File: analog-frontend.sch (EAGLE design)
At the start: 3 parts, among them IC1 ADG731

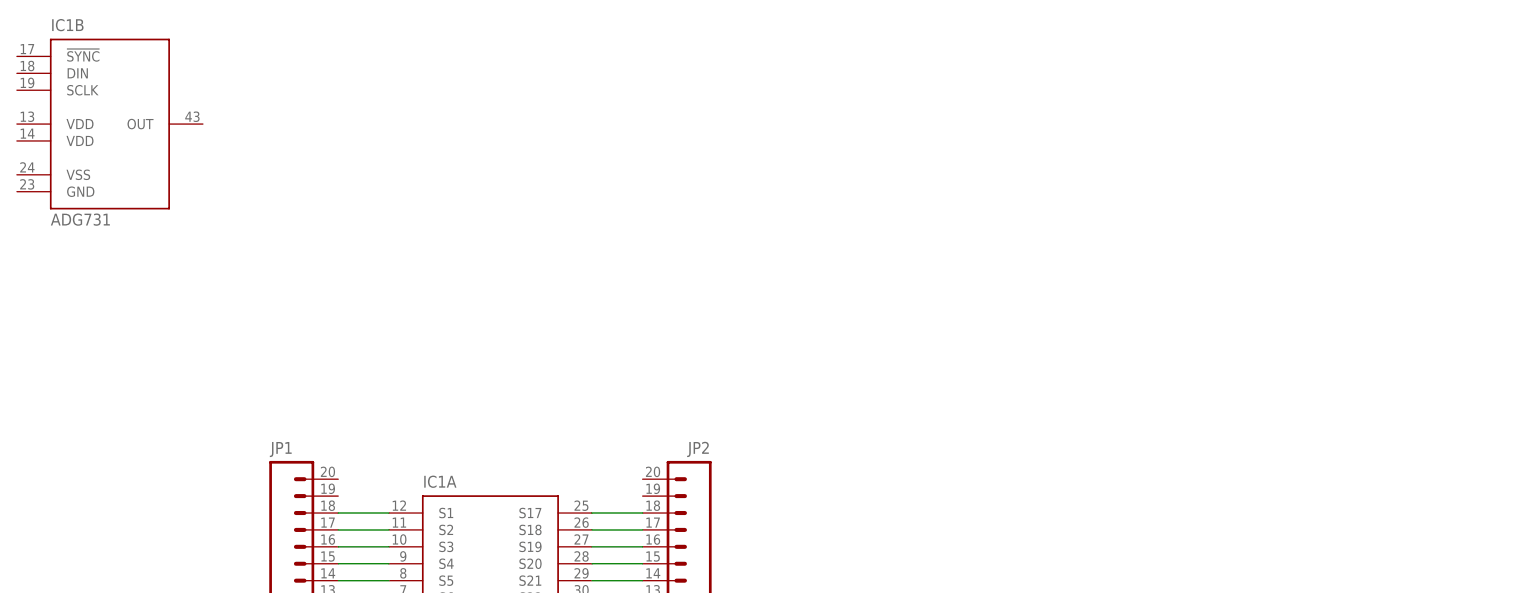
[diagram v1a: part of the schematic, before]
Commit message: added power supply circuit
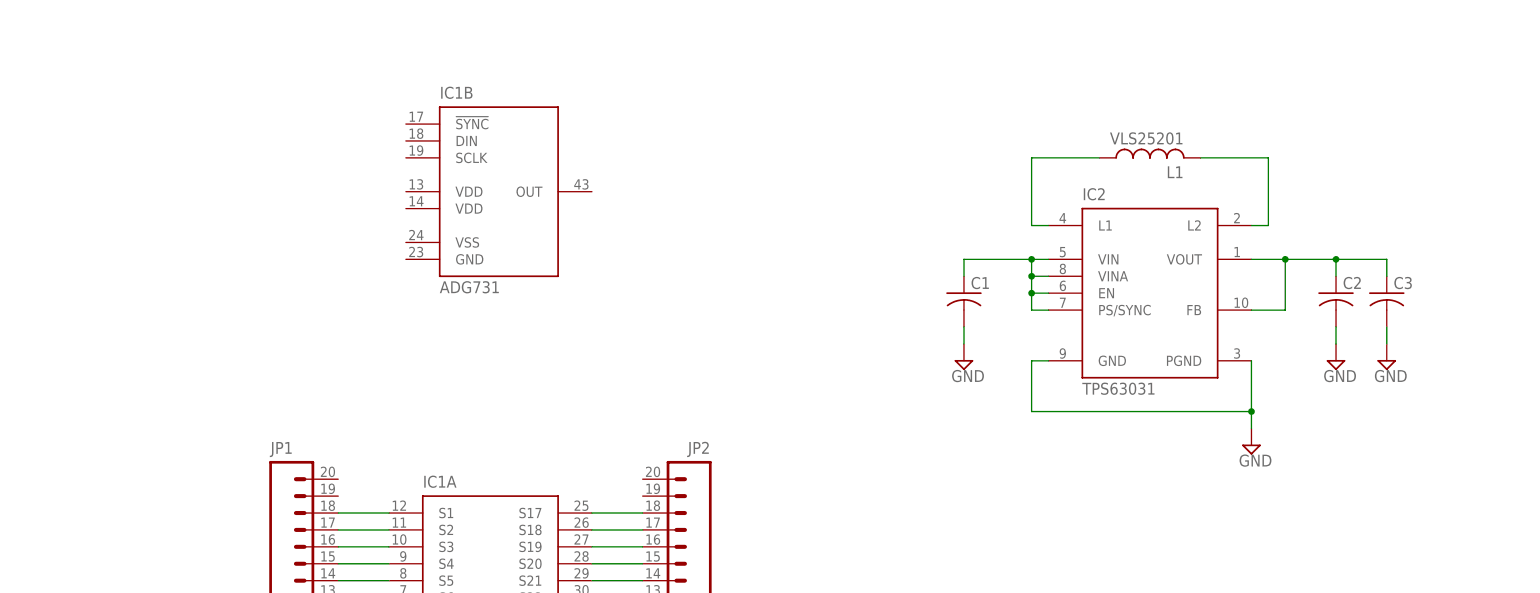
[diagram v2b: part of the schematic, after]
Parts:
- added C1, C2, C3: (no value), rcl:C-USC0402
- added IC2: TPS63031, mor307:TPS63031
- added L1: VLS25201, mor307:VLS25201
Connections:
- new net GND: C1.2, C2.2, C3.2, IC2.GND, IC2.PGND
- new net N$33: IC2.L1, L1.1
- new net N$34: IC2.L2, L1.2
- new net N$35: C1.1, IC2.EN, IC2.PS/SYNC, IC2.VIN, IC2.VINA
- new net N$37: C2.1, C3.1, IC2.FB, IC2.VOUT
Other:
- moved on the sheet: IC1B
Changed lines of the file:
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@@
 <setting verticaltext="up"/>
 </settings>
-<grid distance="0.1" unitdist="inch" unit="inch" style="lines" multiple="1" display="no" altdistance="0.01" altunitdist="inch" altunit="inch"/>
+<grid distance="0.1" unitdist="inch" unit="inch" style="lines" multiple="1" display="yes" altdistance="0.01" altunitdist="inch" altunit="inch"/>
 <layers>
 <layer number="1" name="Top" color="4" fill="1" visible="no" active="no"/>
@@
 <part name="JP2" library="mor307" deviceset="M20" device=""/>
 <part name="IC1" library="mor307" deviceset="ADG731" device=""/>
+<part name="IC2" library="mor307" deviceset="TPS63031" device=""/>
+<part name="L1" library="mor307" deviceset="VLS25201" device=""/>
+<part name="C1" library="rcl" deviceset="C-US" device="C0402"/>
+<part name="C2" library="rcl" deviceset="C-US" device="C0402"/>
+<part name="SUPPLY1" library="supply2" deviceset="GND" device=""/>
+<part name="SUPPLY2" library="supply2" deviceset="GND" device=""/>
+<part name="SUPPLY3" library="supply2" deviceset="GND" device=""/>
+<part name="C3" library="rcl" deviceset="C-US" device="C0402"/>
+<part name="SUPPLY4" library="supply2" deviceset="GND" device=""/>
 </parts>
 <sheets>
@@
 <instance part="JP1" gate="G$1" x="73.66" y="144.78"/>
 <instance part="JP2" gate="G$1" x="139.7" y="144.78" rot="MR0"/>
-<instance part="IC1" gate="B" x="48.26" y="220.98"/>
+<instance part="IC1" gate="B" x="106.68" y="210.82"/>
 <instance part="IC1" gate="A" x="106.68" y="142.24"/>
+<instance part="IC2" gate="G$1" x="205.74" y="195.58"/>
+<instance part="L1" gate="G$1" x="205.74" y="215.9" rot="R90"/>
+<instance part="C1" gate="G$1" x="177.8" y="195.58"/>
+<instance part="C2" gate="G$1" x="233.68" y="195.58"/>
+<instance part="SUPPLY1" gate="GND" x="177.8" y="185.42"/>
+<instance part="SUPPLY2" gate="GND" x="233.68" y="185.42"/>
+<instance part="SUPPLY3" gate="GND" x="220.98" y="172.72"/>
+<instance part="C3" gate="G$1" x="241.3" y="195.58"/>
+<instance part="SUPPLY4" gate="GND" x="241.3" y="185.42"/>
 </instances>
 <busses>
@@
 </segment>
 </net>
+<net name="N$33" class="0">
+<segment>
+<pinref part="IC2" gate="G$1" pin="L1"/>
+<wire x1="190.5" y1="205.74" x2="187.96" y2="205.74" width="0.1524" layer="91"/>
+<wire x1="187.96" y1="205.74" x2="187.96" y2="215.9" width="0.1524" layer="91"/>
+<pinref part="L1" gate="G$1" pin="1"/>
+<wire x1="187.96" y1="215.9" x2="198.12" y2="215.9" width="0.1524" layer="91"/>
+</segment>
+</net>
+<net name="N$34" class="0">
+<segment>
+<pinref part="L1" gate="G$1" pin="2"/>
+<wire x1="213.36" y1="215.9" x2="223.52" y2="215.9" width="0.1524" layer="91"/>
+<wire x1="223.52" y1="215.9" x2="223.52" y2="205.74" width="0.1524" layer="91"/>
+<pinref part="IC2" gate="G$1" pin="L2"/>
+<wire x1="223.52" y1="205.74" x2="220.98" y2="205.74" width="0.1524" layer="91"/>
+</segment>
+</net>
+<net name="N$35" class="0">
+<segment>
+<pinref part="IC2" gate="G$1" pin="PS/SYNC"/>
+<wire x1="190.5" y1="193.04" x2="187.96" y2="193.04" width="0.1524" layer="91"/>
+<wire x1="187.96" y1="193.04" x2="187.96" y2="195.58" width="0.1524" layer="91"/>
+<pinref part="IC2" gate="G$1" pin="VIN"/>
+<wire x1="187.96" y1="195.58" x2="187.96" y2="198.12" width="0.1524" layer="91"/>
+<wire x1="187.96" y1="198.12" x2="187.96" y2="200.66" width="0.1524" layer="91"/>
+<wire x1="187.96" y1="200.66" x2="190.5" y2="200.66" width="0.1524" layer="91"/>
+<pinref part="IC2" gate="G$1" pin="VINA"/>
+<wire x1="190.5" y1="198.12" x2="187.96" y2="198.12" width="0.1524" layer="91"/>
+<junction x="187.96" y="198.12"/>
+<pinref part="IC2" gate="G$1" pin="EN"/>
+<wire x1="190.5" y1="195.58" x2="187.96" y2="195.58" width="0.1524" layer="91"/>
+<junction x="187.96" y="195.58"/>
+<pinref part="C1" gate="G$1" pin="1"/>
+<wire x1="177.8" y1="198.12" x2="177.8" y2="200.66" width="0.1524" layer="91"/>
+<wire x1="177.8" y1="200.66" x2="187.96" y2="200.66" width="0.1524" layer="91"/>
+<junction x="187.96" y="200.66"/>
+</segment>
+</net>
+<net name="N$37" class="0">
+<segment>
+<pinref part="IC2" gate="G$1" pin="VOUT"/>
+<wire x1="220.98" y1="200.66" x2="226.06" y2="200.66" width="0.1524" layer="91"/>
+<pinref part="C2" gate="G$1" pin="1"/>
+<wire x1="226.06" y1="200.66" x2="233.68" y2="200.66" width="0.1524" layer="91"/>
+<wire x1="233.68" y1="200.66" x2="233.68" y2="198.12" width="0.1524" layer="91"/>
+<pinref part="IC2" gate="G$1" pin="FB"/>
+<wire x1="220.98" y1="193.04" x2="226.06" y2="193.04" width="0.1524" layer="91"/>
+<wire x1="226.06" y1="193.04" x2="226.06" y2="200.66" width="0.1524" layer="91"/>
+<junction x="226.06" y="200.66"/>
+<wire x1="233.68" y1="200.66" x2="241.3" y2="200.66" width="0.1524" layer="91"/>
+<junction x="233.68" y="200.66"/>
+<pinref part="C3" gate="G$1" pin="1"/>
+<wire x1="241.3" y1="200.66" x2="241.3" y2="198.12" width="0.1524" layer="91"/>
+</segment>
+</net>
+<net name="GND" class="0">
+<segment>
+<pinref part="SUPPLY1" gate="GND" pin="GND"/>
+<pinref part="C1" gate="G$1" pin="2"/>
+<wire x1="177.8" y1="187.96" x2="177.8" y2="190.5" width="0.1524" layer="91"/>
+</segment>
+<segment>
+<pinref part="C2" gate="G$1" pin="2"/>
+<pinref part="SUPPLY2" gate="GND" pin="GND"/>
+<wire x1="233.68" y1="190.5" x2="233.68" y2="187.96" width="0.1524" layer="91"/>
+</segment>
+<segment>
+<pinref part="IC2" gate="G$1" pin="PGND"/>
+<pinref part="SUPPLY3" gate="GND" pin="GND"/>
+<wire x1="220.98" y1="185.42" x2="220.98" y2="177.8" width="0.1524" layer="91"/>
+<pinref part="IC2" gate="G$1" pin="GND"/>
+<wire x1="220.98" y1="177.8" x2="220.98" y2="175.26" width="0.1524" layer="91"/>
+<wire x1="190.5" y1="185.42" x2="187.96" y2="185.42" width="0.1524" layer="91"/>
+<wire x1="187.96" y1="185.42" x2="187.96" y2="177.8" width="0.1524" layer="91"/>
+<wire x1="187.96" y1="177.8" x2="220.98" y2="177.8" width="0.1524" layer="91"/>
+<junction x="220.98" y="177.8"/>
+</segment>
+<segment>
+<pinref part="C3" gate="G$1" pin="2"/>
+<wire x1="241.3" y1="190.5" x2="241.3" y2="187.96" width="0.1524" layer="91"/>
+<pinref part="SUPPLY4" gate="GND" pin="GND"/>
+</segment>
+</net>

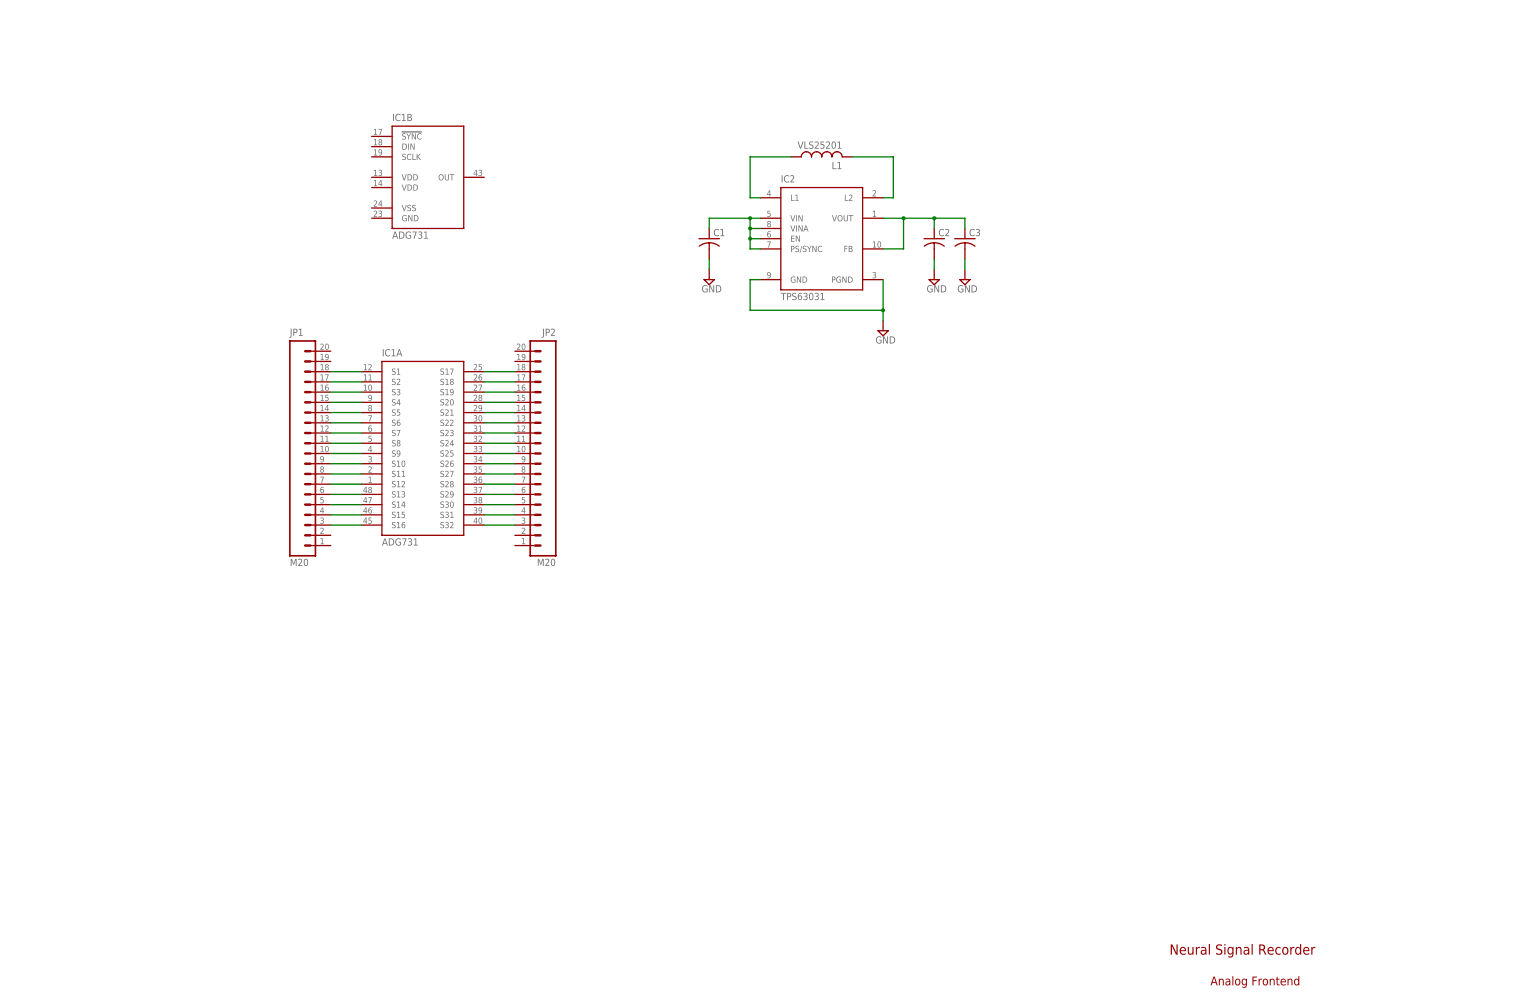
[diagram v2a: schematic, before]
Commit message: added mcu, radio and finished analog frontend
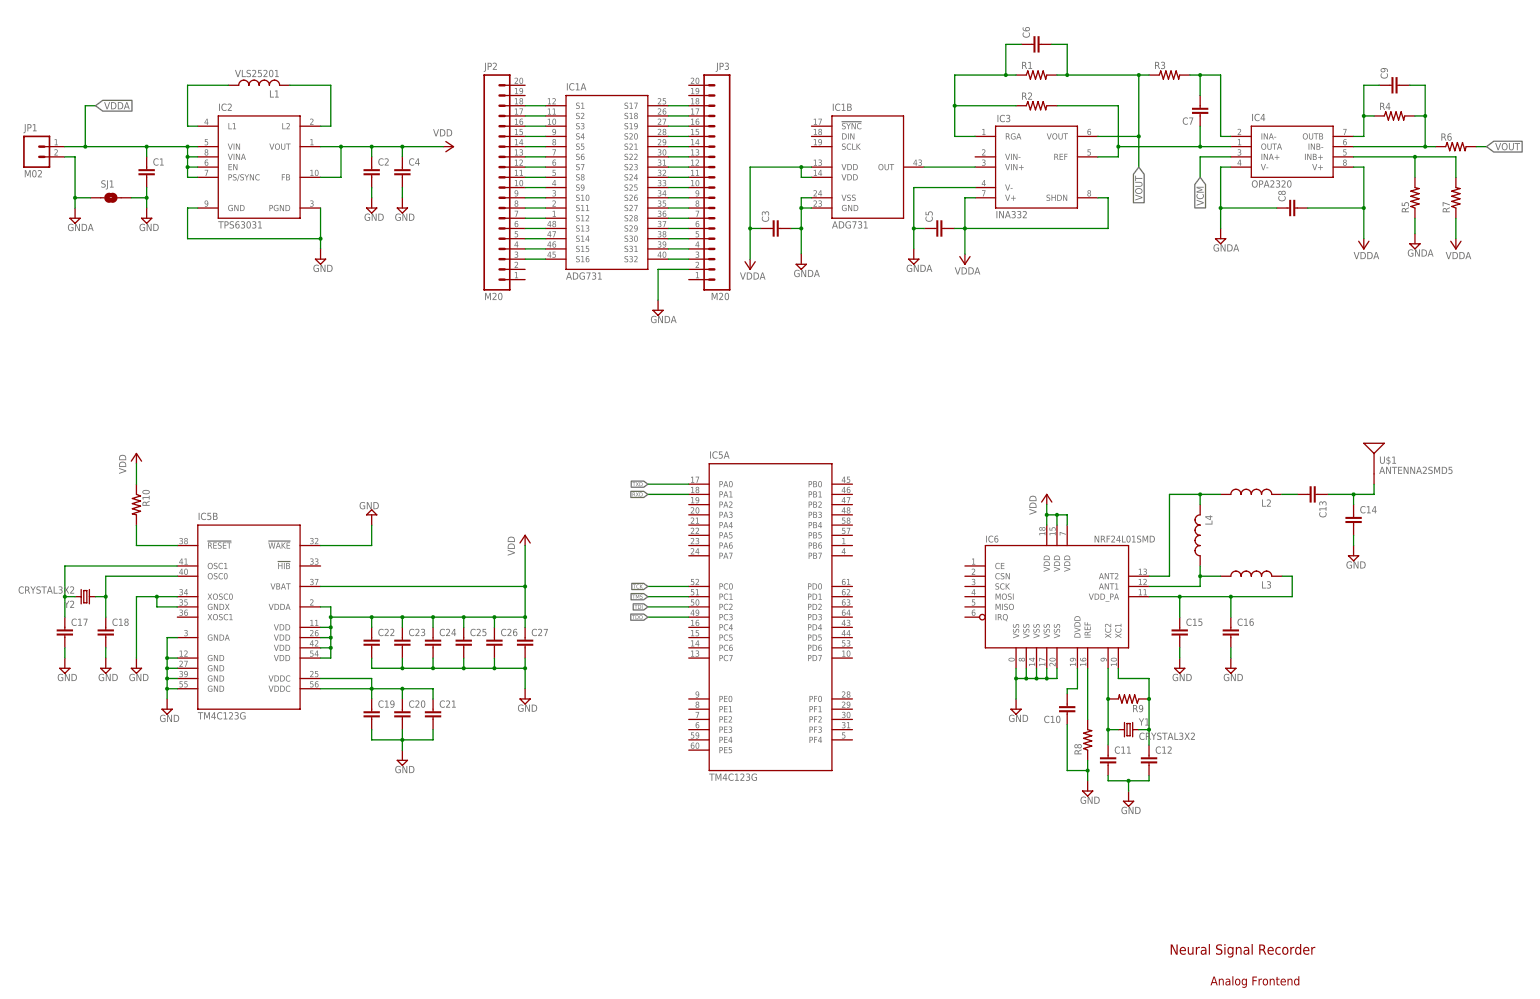
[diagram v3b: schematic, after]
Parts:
- added C10, C11, C12, C13, C14, C15, C16, C17, C18, C19, C20, C22, C23, C24, C25, C26, C27, C4, C5, C6, C7, C8, C9: (no value), rcl:C-EUC0201
- added C21: (no value), rcl:C-EUC0402
- added IC3: INA332, mor307:INA332
- added IC4: OPA2320, mor307:OPA2320
- added IC5: TM4C123G, mor307:TM4C123G
- added IC6: NRF24L01SMD, SparkFun-RF:NRF24L01SMD
- added JP3: M20, mor307:M20
- added L2, L3, L4: (no value), rcl:L-USL0201
- added R1, R10, R2, R3, R4, R5, R6, R7, R8, R9: (no value), rcl:R-US_R0201
- added SJ1: JUMPER-PAD-2-NO, SparkFun-Passives:JUMPER-PAD-2-NO
- added U$1: ANTENNA2SMD5, SparkFun-RF:ANTENNA2SMD5
- added Y1, Y2: CRYSTAL3X2, mor307:CRYSTAL3X2
- C1, C2, C3: device rcl:C-USC0402 -> rcl:C-EUC0201
- JP1: value M20 -> M02; device mor307:M20 -> mor307:M02
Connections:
- new net +3V3: C2.1, C22.1, C23.1, C24.1, C25.1, C26.1, C27.1, C4.1, IC2.FB, IC2.VOUT, IC5B.VBAT, IC5B.VDD@1, IC5B.VDD@2, IC5B.VDD@3, IC5B.VDD@4, IC5B.VDDA, IC6.VDD@15, IC6.VDD@18, IC6.VDD@7, R10.1
- new net GNDA: C3.2, C5.1, C8.1, IC1B.GND, IC1B.VSS, IC3.V-, IC4.V-, JP1.2, JP3.2, R5.1, SJ1.1
- new net N$36: C7.1, IC3.REF, IC4.OUTA, R2.2
- new net N$38: C6.1, IC3.RGA, R1.1, R2.1
- new net N$39: C9.2, IC4.INB-, R4.2, R6.1
- new net N$40: C17.1, IC5B.OSC1, Y2.2
- new net N$41: C9.1, IC4.OUTB, R4.1
- new net N$42: C7.2, IC4.INA-, R3.2
- new net N$43: C10.2, IC6.DVDD
- new net N$44: IC6.IREF, R8.2
- new net N$45: C19.1, C20.1, C21.1, IC5B.VDDC@1, IC5B.VDDC@2
- new net N$46: C11.1, IC6.XC2, R9.2, Y1.1
- new net N$47: IC4.INB+, R5.2, R7.2
- new net N$48: C12.1, IC6.XC1, R9.1, Y1.2
- new net N$49: IC5B.!RESET!, R10.2
- new net N$50: IC6.ANT1, L3.1, L4.1
- new net N$51: IC6.ANT2, L2.1, L4.2
- new net N$52: C15.1, C16.1, IC6.VDD_PA, L3.2
- new net N$53: C13.2, L2.2
- new net N$54: C13.1, C14.1, U$1.SIGNAL
- new net RXD: IC5A.PA1
- new net TCK: IC5A.PC0
- new net TDI: IC5A.PC2
- new net TDO: IC5A.PC3
- new net TMS: IC5A.PC1
- new net TXD: IC5A.PA0
- new net VCM: IC4.INA+
- new net VDDA: C1.1, C3.1, C5.2, C8.2, IC1B.VDD@1, IC1B.VDD@2, IC2.EN, IC2.PS/SYNC, IC2.VIN, IC2.VINA, IC3.SHDN, IC3.V+, IC4.V+, JP1.1, R7.1
- new net VOUT: C6.2, IC3.VOUT, R1.2, R3.1, R6.2
- net GND: now also C10.1, C11.2, C12.2, C14.2, C15.2, C16.2, C17.2, C18.2, C19.2, C20.2, C21.2, C22.2, C23.2, C24.2, C25.2, C26.2, C27.2, C4.2, IC5B.!WAKE!, IC5B.GND@1, IC5B.GND@2, IC5B.GND@3, IC5B.GND@4, IC5B.GNDA, IC5B.GNDX, IC5B.XOSC0, IC6.VSS@0, IC6.VSS@14, IC6.VSS@17, IC6.VSS@20, IC6.VSS@8, R8.1, SJ1.2; no longer C3.2
- net N$1: now also JP2.18; no longer JP1.18
- net N$10: now also JP2.12; no longer JP1.12
- net N$11: now also JP2.11; no longer JP1.11
- net N$12: now also JP2.10; no longer JP1.10
- net N$13: now also JP2.9; no longer JP1.9
- net N$14: now also JP2.8; no longer JP1.8
- net N$15: now also JP2.7; no longer JP1.7
- net N$16: now also JP2.6; no longer JP1.6
- net N$17: now also JP2.5; no longer JP1.5
- net N$18: now also JP2.4; no longer JP1.4
- net N$19: now also JP3.17; no longer JP2.17
- net N$2: now also JP2.3; no longer JP1.3
- net N$20: now also JP3.16; no longer JP2.16
- net N$21: now also JP3.15; no longer JP2.15
- net N$22: now also JP3.14; no longer JP2.14
- net N$23: now also JP3.13; no longer JP2.13
- net N$24: now also JP3.12; no longer JP2.12
- net N$25: now also JP3.11; no longer JP2.11
- net N$26: now also JP3.10; no longer JP2.10
- net N$27: now also JP3.9; no longer JP2.9
- net N$28: now also JP3.8; no longer JP2.8
- net N$29: now also JP3.7; no longer JP2.7
- net N$3: now also JP3.18; no longer JP2.18
- net N$30: now also JP3.6; no longer JP2.6
- net N$31: now also JP3.5; no longer JP2.5
- net N$32: now also JP3.4; no longer JP2.4
- net N$35: now also IC1B.OUT, IC3.VIN+; no longer C1.1, IC2.EN, IC2.PS/SYNC, IC2.VIN, IC2.VINA
- net N$37: now also C18.1, IC5B.OSC0, Y2.1; no longer C2.1, C3.1, IC2.FB, IC2.VOUT
- net N$4: now also JP3.3; no longer JP2.3
- net N$5: now also JP2.17; no longer JP1.17
- net N$6: now also JP2.16; no longer JP1.16
- net N$7: now also JP2.15; no longer JP1.15
- net N$8: now also JP2.14; no longer JP1.14
- net N$9: now also JP2.13; no longer JP1.13
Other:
- moved on the sheet: C1, C2, C3, IC1A, IC1B, IC2, JP2, L1

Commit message: routing complete!
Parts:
- removed SJ1: JUMPER-PAD-2-NO, SparkFun-Passives:JUMPER-PAD-2-NO
- added C28: (no value), rcl:C-EUC0201
- added R11, R12, R13, R14: (no value), rcl:R-US_R0201
- added TP1, TP2, TP3, TP4, TP5, TP6, TP7, TP8, TP9: PTR1B1,27, testpad:PTR1B1,27
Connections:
- new net N$55: IC5A.PD0, IC6.SCK
- new net N$56: IC5A.PD1, IC6.CSN
- new net N$58: IC5A.PD2, IC6.MISO
- new net N$59: IC5A.PB6, IC6.CE
- new net N$60: IC5A.PB4, IC6.IRQ
- new net N$61: IC5A.PD3, IC6.MOSI
- new net N$62: C28.1, IC3.VIN-, R14.1
- new net PF1: IC1B.DIN, IC5A.PF1
- new net PF2: IC1B.SCLK, IC5A.PF2
- new net PF3: IC1B.!SYNC!, IC5A.PF3
- new net VCM1: IC4.INA+, JP2.1
- new net VCM2: JP2.20, R14.2
- new net VREF: C28.2, JP2.19
- net +3V3: now also TP8.TP
- net GND: now also R13.2, TP9.TP; no longer SJ1.2
- net GNDA: now also JP2.2, R12.2, R13.1; no longer JP3.2, SJ1.1
- net N$49: now also TP7.TP
- net RXD: now also TP1.TP
- net TCK: now also TP3.TP
- net TDI: now also TP5.TP
- net TDO: now also TP6.TP
- net TMS: now also TP4.TP
- net TXD: now also TP2.TP
- net VCM: now also JP3.1, R11.2, R12.1; no longer IC4.INA+
- net VDDA: now also R11.1
